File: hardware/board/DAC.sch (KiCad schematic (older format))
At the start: 7 parts, among them U6 AD5685R?RUZ

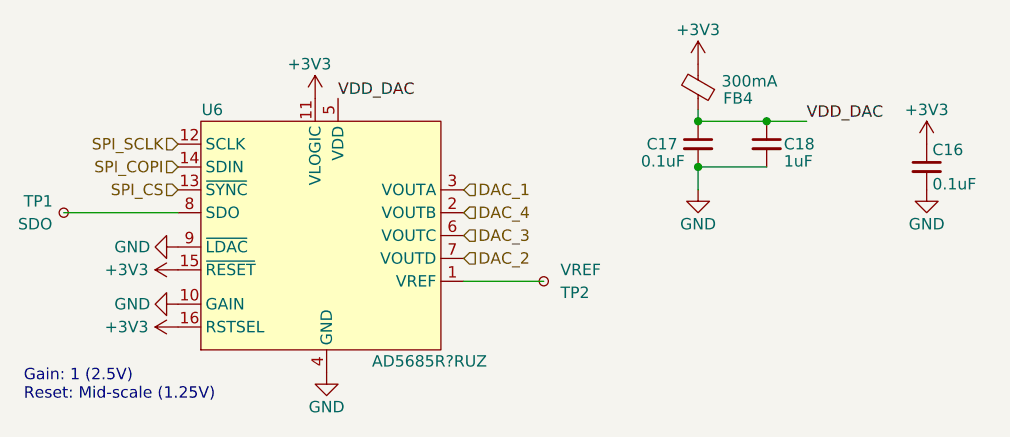
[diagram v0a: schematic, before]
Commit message: More updates to the board design
- Added polyfuses for downstream power
- Added breakout header for external, panel-mounted USB port
- Added I/O breakout for the switches and buttons on the front control panel
- Made the MCU footprint a hybrid QFP/QFN footprint
- Add a nice illustration to the board backside
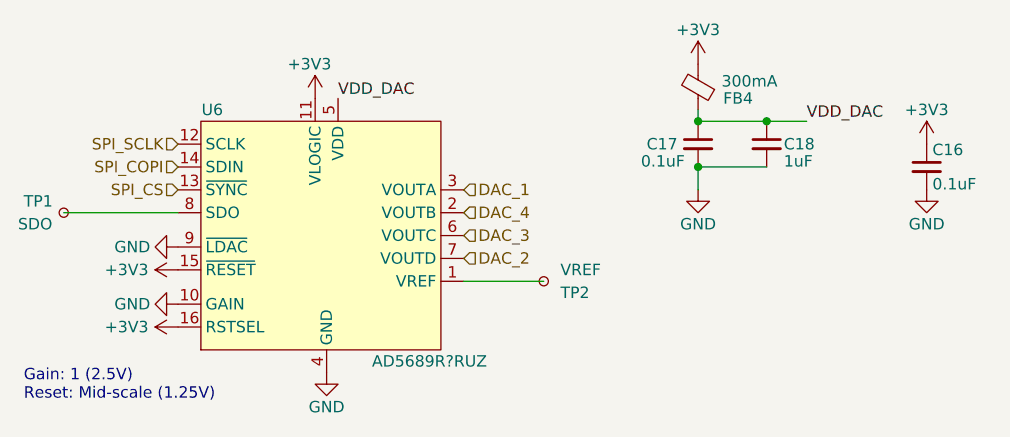
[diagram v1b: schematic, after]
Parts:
- U6: value AD5685R?RUZ -> AD5689R?RUZ
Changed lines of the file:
@@
 Sheet 6 7
 Title "Hubble Motherboard"
-Date "2021-11-12"
+Date "2021-11-20"
 Rev "v2"
 Comp "Winterbloom"
 Comment1 "Alethea Flowers"
 Comment2 "CERN-OHL-P V2"
-Comment3 ""
+Comment3 "hubble.wntr.dev"
 Comment4 ""
 $EndDescr
@@
 AR Path="/617FCAA5/6180A7CC" Ref="U6"  Part="1"
 F 0 "U6" H 2000 3325 50  0000 C CNN
-F 1 "AD5685R?RUZ" H 2950 2225 50  0000 C CNN
+F 1 "AD5689R?RUZ" H 2950 2225 50  0000 C CNN
 F 2 "Package_SO:TSSOP-16_4.4x5mm_P0.65mm" H 2500 4125 50  0001 C CNN
 F 3 "https://www.analog.com/media/en/technical-documentation/data-sheets/ad5686r_5685r_5684r.pdf" H 2550 2775 50  0001 C CNN
